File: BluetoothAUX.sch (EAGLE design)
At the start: 19 parts, among them IC2 TPA6132A2, J3 AUDIO_JACK_TRRSSMD_RA, J4 USB, Q1 FDV301N

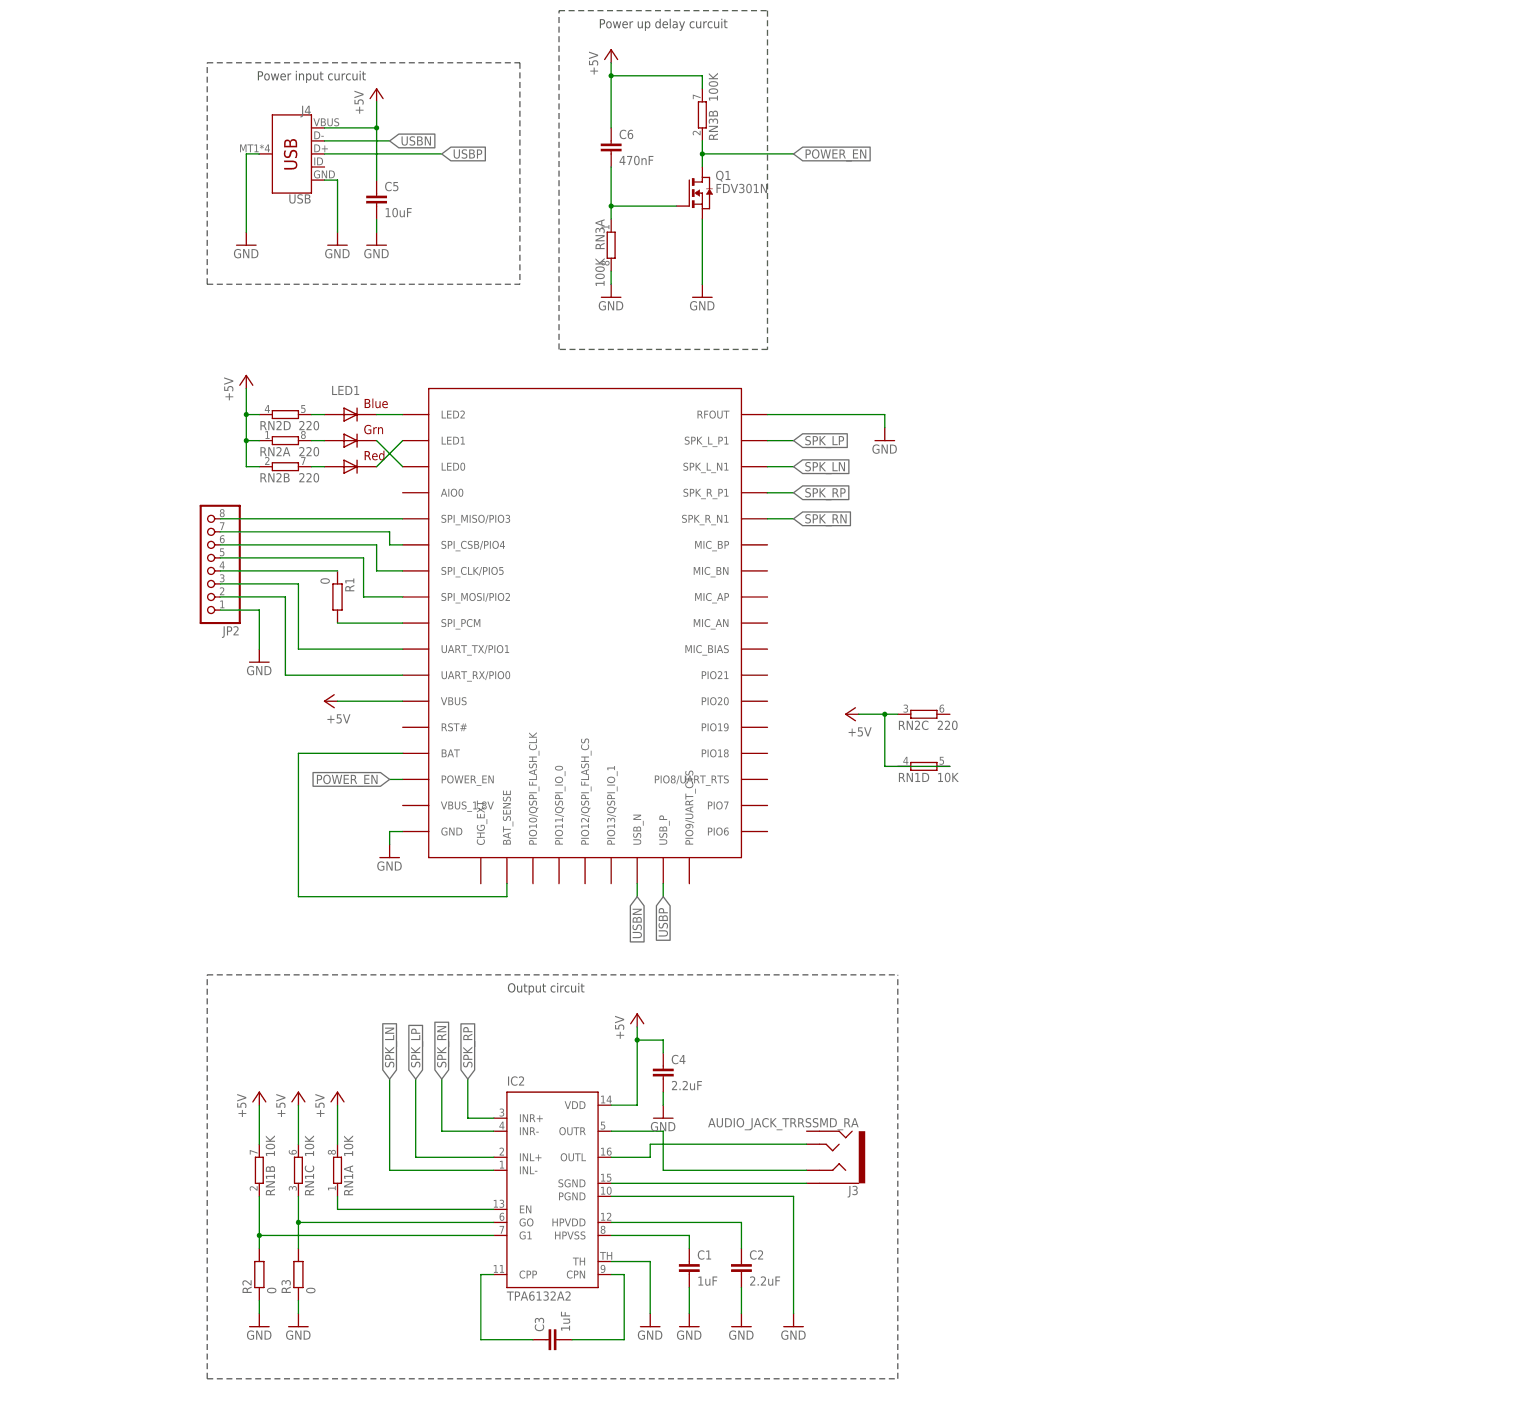
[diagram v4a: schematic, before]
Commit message: DIP switch, 4-pin LED, Powerup fix
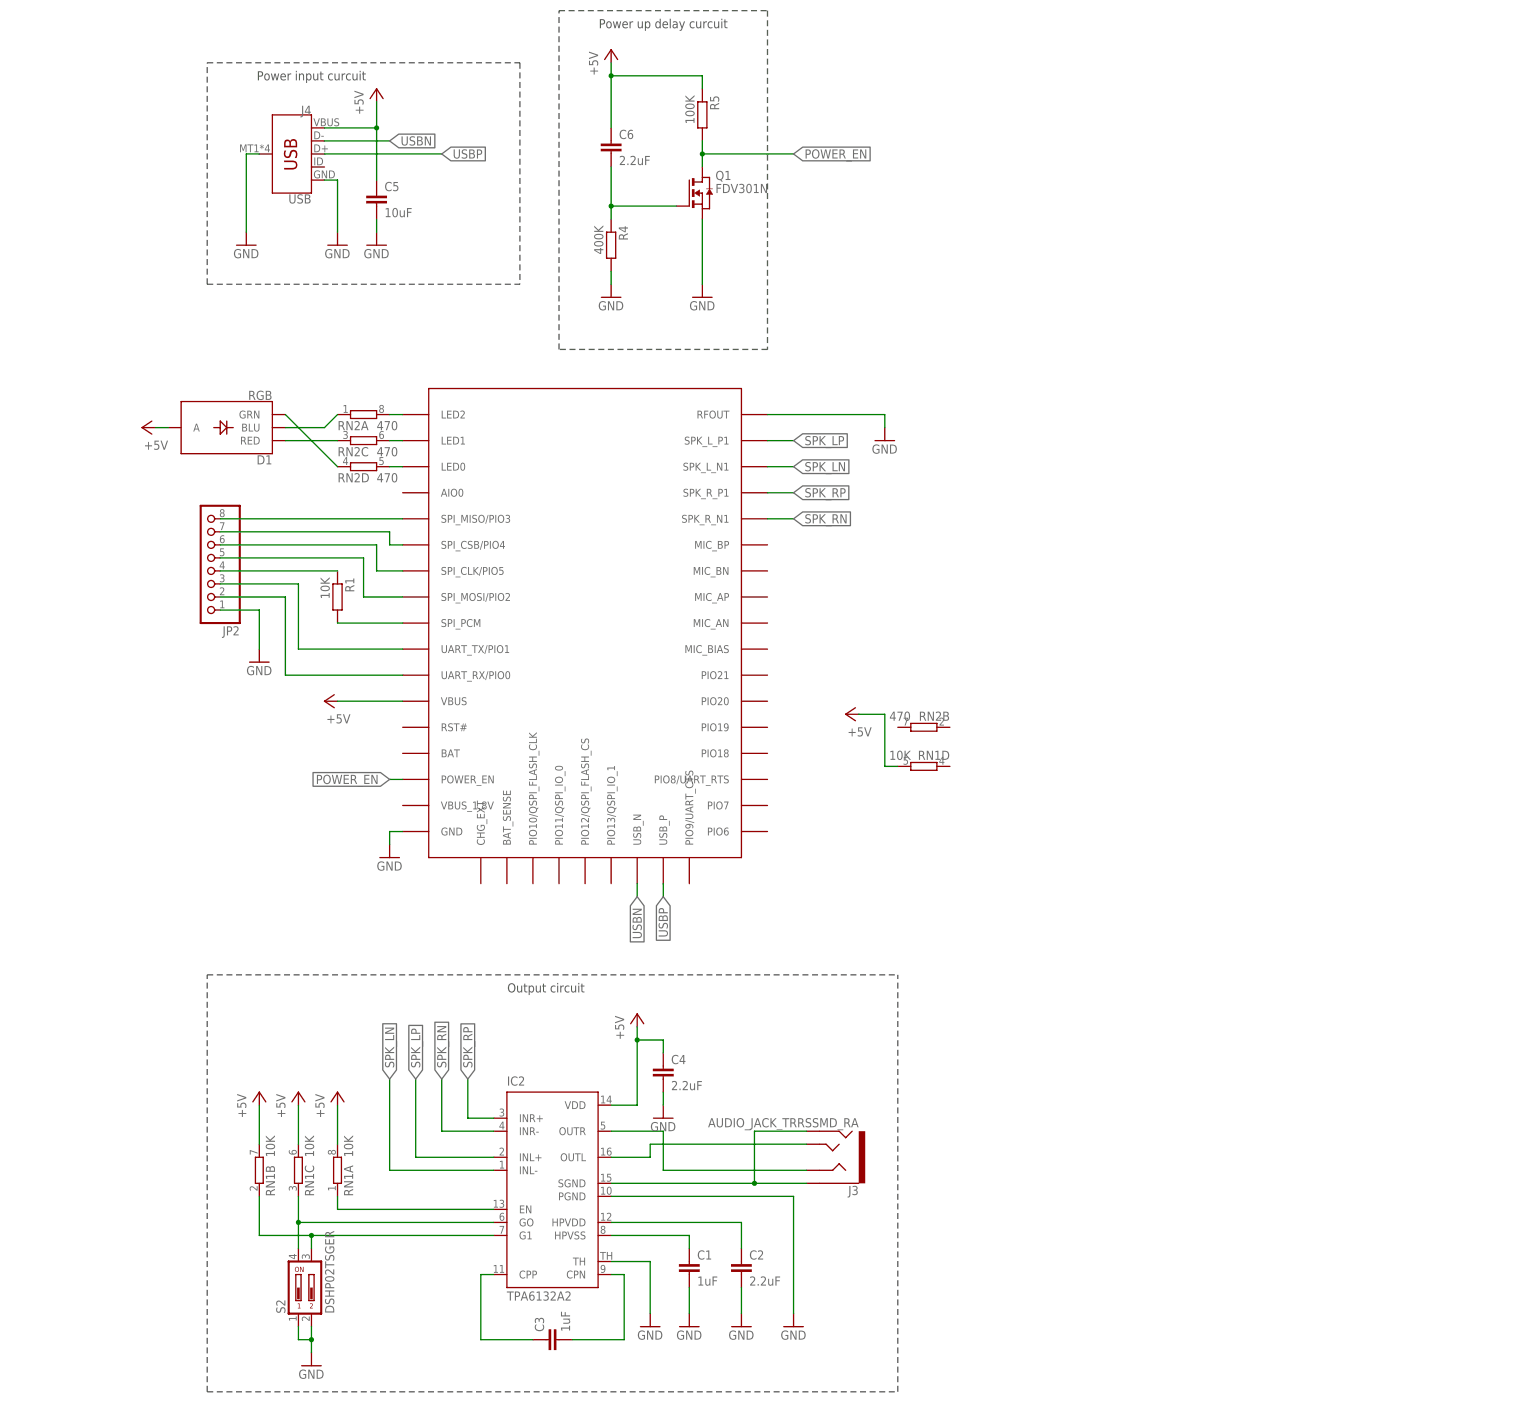
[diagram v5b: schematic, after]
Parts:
- removed LED1: RGBLED5050, adafruit:RGBLED5050
- removed R2, R3: 0, resistor:R-EU_R0603
- removed RN3: 100K, resistor-dil:4R-N0603-ARC
- added D1: RGB, SparkFun-LED:LED-RGB-CAPLCC
- added R4: 400K, resistor:R-EU_R0603
- added R5: 100K, resistor:R-EU_R0603
- added S2: DSHP02TSGER, BluetoothAUX:DSHP02TSGER
- C6: value 470nF -> 2.2uF
- R1: value 0 -> 10K
- RN2: value 220 -> 470
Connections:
- removed net LED_B: LED1.BLUE_A, RN2D.2
- removed net LED_G: LED1.GREEN_A, RN2A.2
- removed net LED_R: LED1.RED_A, RN2B.2
- removed net VBAT_SENSE: U$1.BAT, U$1.BAT_SENSE
- new net BLUE: RN2A.2, U$1.LED2
- new net GREEN: RN2D.2, U$1.LED0
- new net RED: RN2C.2, U$1.LED1
- net +5V: now also D1.A, R5.1; no longer RN2A.1, RN2B.1, RN2C.1, RN2D.1, RN3B.2
- net G0: now also S2.4; no longer R3.2
- net G1: now also S2.3; no longer R2.2
- net GND: now also R4.2, S2.1, S2.2; no longer R2.1, R3.1, RN3A.2
- net N$2: now also D1.GRN, RN2D.1; no longer LED1.GREEN_C, U$1.LED0
- net N$3: now also D1.RED, RN2C.1; no longer LED1.RED_C, U$1.LED1
- net N$4: now also D1.BLU, RN2A.1; no longer LED1.BLUE_C, U$1.LED2
- net N$5: now also R4.1; no longer RN3A.1
- net POWER_EN: now also R5.2; no longer RN3B.1
- net SGND: now also J3.RING2
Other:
- moved on the sheet: RN1D, RN2A, RN2B, RN2C, RN2D

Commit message: Remove UART, add silk
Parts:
- removed JP2: (no value), pinhead:PINHD-1X8
- added JP1: (no value), pinhead:PINHD-1X7
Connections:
- removed net RX: JP2.2, U$1.UART_RX/PIO0
- removed net SPI_PCM: JP2.4, R1.1
- removed net TX: JP2.3, U$1.UART_TX/PIO1
- new net N$6: JP1.2, R1.1
- net +5V: now also JP1.1
- net CLK: now also JP1.5; no longer JP2.6
- net CS: now also JP1.6; no longer JP2.7
- net GND: now also JP1.3; no longer JP2.1
- net MISO: now also JP1.7; no longer JP2.8
- net MOSI: now also JP1.4; no longer JP2.5
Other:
- moved on the sheet: R1
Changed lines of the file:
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@@
 <part name="GND9" library="supply1" deviceset="GND" device=""/>
 <part name="P+1" library="supply1" deviceset="+5V" device=""/>
-<part name="JP2" library="pinhead" library_urn="urn:adsk.eagle:library:325" deviceset="PINHD-1X8" device="" package3d_urn="urn:adsk.eagle:package:22409/2"/>
 <part name="C6" library="resistor" library_urn="urn:adsk.eagle:library:348" deviceset="C-EU" device="C0603" package3d_urn="urn:adsk.eagle:package:26138/1" value="2.2uF"/>
 <part name="GND2" library="supply1" deviceset="GND" device=""/>
@@
 <part name="S2" library="BluetoothAUX" deviceset="DSHP02TSGER" device=""/>
 <part name="D1" library="SparkFun-LED" deviceset="LED-RGB-CA" device="PLCC" value="RGB"/>
+<part name="JP1" library="pinhead" library_urn="urn:adsk.eagle:library:325" deviceset="PINHD-1X7" device="" package3d_urn="urn:adsk.eagle:package:22477/1"/>
+<part name="P+10" library="supply1" deviceset="+5V" device=""/>
 </parts>
 <sheets>
@@
 <instance part="GND5" gate="1" x="-38.1" y="40.64"/>
 <instance part="GND6" gate="1" x="-144.78" y="78.74"/>
-<instance part="GND7" gate="1" x="-160.02" y="-2.54"/>
+<instance part="GND7" gate="1" x="-157.48" y="-2.54"/>
 <instance part="GND3" gate="1" x="-134.62" y="-40.64"/>
 <instance part="P+3" gate="1" x="-147.32" y="-10.16" rot="R90"/>
@@
 <instance part="GND9" gate="1" x="-83.82" y="-132.08"/>
 <instance part="P+1" gate="1" x="-182.88" y="43.18" rot="R90"/>
-<instance part="JP2" gate="A" x="-170.18" y="17.78" rot="R180"/>
 <instance part="C6" gate="G$1" x="-91.44" y="99.06"/>
 <instance part="GND2" gate="1" x="-91.44" y="68.58"/>
@@
 <instance part="RN1" gate="D" x="-30.48" y="-22.86" rot="R180"/>
 <instance part="RN2" gate="B" x="-30.48" y="-15.24" rot="R180"/>
-<instance part="P+9" gate="1" x="-45.72" y="-12.7" rot="R90"/>
-<instance part="R1" gate="G$1" x="-144.78" y="10.16" rot="R270"/>
+<instance part="P+9" gate="1" x="-40.64" y="-22.86" rot="R90"/>
+<instance part="R1" gate="G$1" x="-139.7" y="5.08"/>
 <instance part="R4" gate="G$1" x="-91.44" y="78.74" rot="R270"/>
 <instance part="R5" gate="G$1" x="-73.66" y="104.14" rot="R270"/>
 <instance part="S2" gate="G$1" x="-152.4" y="-124.46"/>
 <instance part="D1" gate="G$1" x="-165.1" y="43.18" rot="R180"/>
+<instance part="JP1" gate="A" x="-167.64" y="17.78" rot="R180"/>
+<instance part="P+10" gate="1" x="-154.94" y="33.02"/>
 </instances>
 <busses>
@@
 <segment>
 <pinref part="GND7" gate="1" pin="GND"/>
-<wire x1="-160.02" y1="7.62" x2="-160.02" y2="0" width="0.1524" layer="91"/>
-<pinref part="JP2" gate="A" pin="1"/>
-<wire x1="-167.64" y1="7.62" x2="-160.02" y2="7.62" width="0.1524" layer="91"/>
+<wire x1="-157.48" y1="15.24" x2="-157.48" y2="0" width="0.1524" layer="91"/>
+<pinref part="JP1" gate="A" pin="3"/>
+<wire x1="-165.1" y1="15.24" x2="-157.48" y2="15.24" width="0.1524" layer="91"/>
 </segment>
 <segment>
@@
 <segment>
 <pinref part="P+9" gate="1" pin="+5V"/>
-<wire x1="-43.18" y1="-12.7" x2="-38.1" y2="-12.7" width="0.1524" layer="91"/>
 <pinref part="RN1" gate="D" pin="2"/>
 <wire x1="-35.56" y1="-22.86" x2="-38.1" y2="-22.86" width="0.1524" layer="91"/>
-<wire x1="-38.1" y1="-22.86" x2="-38.1" y2="-12.7" width="0.1524" layer="91"/>
+</segment>
+<segment>
+<wire x1="-154.94" y1="10.16" x2="-154.94" y2="30.48" width="0.1524" layer="91"/>
+<pinref part="P+10" gate="1" pin="+5V"/>
+<pinref part="JP1" gate="A" pin="1"/>
+<wire x1="-165.1" y1="10.16" x2="-154.94" y2="10.16" width="0.1524" layer="91"/>
 </segment>
 </net>
@@
 <segment>
 <pinref part="U$1" gate="G$1" pin="SPI_MISO/PIO3"/>
-<pinref part="JP2" gate="A" pin="8"/>
-<wire x1="-167.64" y1="25.4" x2="-132.08" y2="25.4" width="0.1524" layer="91"/>
+<pinref part="JP1" gate="A" pin="7"/>
+<wire x1="-165.1" y1="25.4" x2="-132.08" y2="25.4" width="0.1524" layer="91"/>
 </segment>
 </net>
@@
 <pinref part="U$1" gate="G$1" pin="SPI_CSB/PIO4"/>
 <wire x1="-132.08" y1="20.32" x2="-134.62" y2="20.32" width="0.1524" layer="91"/>
-<wire x1="-167.64" y1="22.86" x2="-134.62" y2="22.86" width="0.1524" layer="91"/>
+<wire x1="-165.1" y1="22.86" x2="-134.62" y2="22.86" width="0.1524" layer="91"/>
 <wire x1="-134.62" y1="22.86" x2="-134.62" y2="20.32" width="0.1524" layer="91"/>
-<pinref part="JP2" gate="A" pin="7"/>
+<pinref part="JP1" gate="A" pin="6"/>
 </segment>
 </net>
@@
 <pinref part="U$1" gate="G$1" pin="SPI_CLK/PIO5"/>
 <wire x1="-137.16" y1="15.24" x2="-132.08" y2="15.24" width="0.1524" layer="91"/>
-<wire x1="-167.64" y1="20.32" x2="-137.16" y2="20.32" width="0.1524" layer="91"/>
+<wire x1="-165.1" y1="20.32" x2="-137.16" y2="20.32" width="0.1524" layer="91"/>
 <wire x1="-137.16" y1="20.32" x2="-137.16" y2="15.24" width="0.1524" layer="91"/>
-<pinref part="JP2" gate="A" pin="6"/>
+<pinref part="JP1" gate="A" pin="5"/>
 </segment>
 </net>
@@
 <pinref part="U$1" gate="G$1" pin="SPI_MOSI/PIO2"/>
 <wire x1="-139.7" y1="10.16" x2="-132.08" y2="10.16" width="0.1524" layer="91"/>
-<wire x1="-167.64" y1="17.78" x2="-139.7" y2="17.78" width="0.1524" layer="91"/>
+<wire x1="-165.1" y1="17.78" x2="-139.7" y2="17.78" width="0.1524" layer="91"/>
 <wire x1="-139.7" y1="17.78" x2="-139.7" y2="10.16" width="0.1524" layer="91"/>
-<pinref part="JP2" gate="A" pin="5"/>
-</segment>
-</net>
-<net name="TX" class="0">
-<segment>
-<pinref part="U$1" gate="G$1" pin="UART_TX/PIO1"/>
-<wire x1="-132.08" y1="0" x2="-152.4" y2="0" width="0.1524" layer="91"/>
-<wire x1="-152.4" y1="12.7" x2="-152.4" y2="0" width="0.1524" layer="91"/>
-<pinref part="JP2" gate="A" pin="3"/>
-<wire x1="-167.64" y1="12.7" x2="-152.4" y2="12.7" width="0.1524" layer="91"/>
-</segment>
-</net>
-<net name="RX" class="0">
-<segment>
-<pinref part="U$1" gate="G$1" pin="UART_RX/PIO0"/>
-<wire x1="-132.08" y1="-5.08" x2="-154.94" y2="-5.08" width="0.1524" layer="91"/>
-<wire x1="-154.94" y1="10.16" x2="-154.94" y2="-5.08" width="0.1524" layer="91"/>
-<pinref part="JP2" gate="A" pin="2"/>
-<wire x1="-167.64" y1="10.16" x2="-154.94" y2="10.16" width="0.1524" layer="91"/>
+<pinref part="JP1" gate="A" pin="4"/>
 </segment>
 </net>
@@
 </segment>
 </net>
-<net name="SPI_PCM" class="0">
-<segment>
-<pinref part="JP2" gate="A" pin="4"/>
-<wire x1="-167.64" y1="15.24" x2="-144.78" y2="15.24" width="0.1524" layer="91"/>
-<pinref part="R1" gate="G$1" pin="1"/>
-</segment>
-</net>
 <net name="N$2" class="0">
 <segment>
@@
 <pinref part="U$1" gate="G$1" pin="SPI_PCM"/>
 <pinref part="R1" gate="G$1" pin="2"/>
-<wire x1="-144.78" y1="5.08" x2="-132.08" y2="5.08" width="0.1524" layer="91"/>
+<wire x1="-134.62" y1="5.08" x2="-132.08" y2="5.08" width="0.1524" layer="91"/>
 </segment>
 </net>
@@
 </segment>
 </net>
+<net name="N$6" class="0">
+<segment>
+<pinref part="JP1" gate="A" pin="2"/>
+<wire x1="-165.1" y1="12.7" x2="-147.32" y2="12.7" width="0.1524" layer="91"/>
+<wire x1="-147.32" y1="12.7" x2="-147.32" y2="5.08" width="0.1524" layer="91"/>
+<pinref part="R1" gate="G$1" pin="1"/>
+<wire x1="-147.32" y1="5.08" x2="-144.78" y2="5.08" width="0.1524" layer="91"/>
+</segment>
+</net>
